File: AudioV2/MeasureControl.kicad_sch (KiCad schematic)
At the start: 107 parts, among them J1601 AUDIO, J1602 V_IN, J1603 15_V_IN, SW1601 DEST sense (3PDT 3rd pole, sa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, U1601 OPA1656, U1602 OPA1656, U1603 LT1763-3.3, U1605 TPS3307-33, U1606 LT1763-5, U1607 BP5293-50, U1608 OPA1656, U1609 XC8107AC20MR-G, U1610 MCP23017 (UI 0x22), U1611 OPA1656, Y1601 ASFL1-12.288MHZ-EC-T

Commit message: AudioV2: HP バッファを移設し、PT2314E の DGND を A_GND へ寄せて I²C にレベルシフタを入れた
未実装のまま「確定」に留まっていた2件を回路図に入れ、注釈・BOM の腐りを直した。

- HP バッファ移設（2026-09-06 確定）: legacy/OutputStage に U501（DIP-8 ソケット、
  標準実装 OPA1652）+ R501/R502 10Ω + C501/C502 470µF NP + R503/R504 100k +
  C503-C506。RV501 ワイパー側のラベルを PHONE_BUF_L/R に改名し、PHONE_L/R は
  バッファ出力になった。J_HP501 / J_LINE501 を 01x03（L / A_GND / R）にして帰路を入れた
- DGND→A_GND ＋ I²C 境界（2026-09-07 確定）: U402.25 を A_GND へ。境界は BSS138 ×2 の
  双方向レベルシフタ（Q401/Q402、PT 側 R412/R413 10k → VCC_TONE）。P82B96 を使わない
  理由（Sx 側 VOL 0.8–1.0 V が PT2314E VIL 1.0 V / RP2350 VIL 0.8 V を食い切る）は
  DECISIONS の実装節に一次資料の数字で置いた
- MeasureControl の注釈: 上書きしてしまった Pico ピン配置ノートを復元（GP9=NC）、
  R1605 / 3.3k の旧記述を消し、U1611 Description を実値（約30k・−115.5 dB）に直した
- NT1603 を in_bom no に揃え、PARTS.md は 385（ネットリスト 389 − NetTie 4）
- DECISIONS: PPTC「戻さない」の理由を言い直し（1・2行目は判定材料にならない、
  3行目の条件は X7R 割れに限らない、U201 の OCP は 230 % max @ nom. VIN 24 V）、
  ヘッドルーム −0.4 dBFS は typ 基準で余裕の確定ではないと追記（7.5k 案を併記）、
  U1611 の 47Ω 省略に CL 100 pF の根拠を足した

検証: check_sexpr 0 / roundtrip 全 OK / 再生成は冪等（バイト一致）/ ERC 11 件（型・件数とも
変化なし）/ ネットリスト 389 個・重複 0・フットプリント未設定 0 / 母板で座標の偶然一致なし

Co-Authored-By: Claude Fable 5.1 <noreply@anthropic.com>
Claude-Session: https://claude.ai/code/session_01VCArLcCGbMGgxvWJ5HFJiY
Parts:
- NT1603: now left out of the parts list
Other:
- note added: "A3 Pico2 横置き: 南列 1-20 西→東 / 北列 21-40 東→西。VSYS=+5V_D via D1601 ショットキ, GND=D_GND | GP0=ADC_DATA GP1=ADC_BCK GP2=ADC_LRCK | GP3/GP4=NC(旧 LCD SPI) | GP5=LCD_CS GP6=LCD_DC GP7=LCD_RST GP8=LCD_EN | GP9=NC（旧 MCLK_SENSE、2026-09-07 削除） | GP10=TP_SDA GP11=TP_SCL GP12=TP_INT GP13=TP_RST | GP15=ADC_nMR (TPS3307 ~MR, OD, H は駆動しない) | GP16=ENC_INTA GP17=ENC_INTB (U1610 MCP23017 割り込み) | GP18=LCD_SCK GP19=LCD_MOS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"
- note added: "OPA2134 からの OPA1656 置き換え。6.19k/4.7k 網（前段入力抵抗は 2026-09-07 に 3.3k→6.19k）では FET 入力が有利。試作で安定性とフルスケール・レベルを確認すること。"
- note added: "POWER/DIGITAL（2026-09-07）: +15V → U1603(+3V3_A) と U1606(+5V_A, SHDN=+3V3_A)。旧 U1604(MBC2596) は削除。U1607=+5V_D（PD_12V_MEAS から）。D1601 ショットキ: +5V_D → Pico VSYS（USB 逆流止め）。Y1601 12.288MHz → R1604 33Ω → SCKI。U1609 XC8107 → LCD_VCC。U1605 TPS3307 監視。"
- note removed: "OPA2134 からの OPA1656 置き換え。3.3k/4.7k 網では FET 入力が有利。試作で安定性とフルスケール・レベルを確認すること。"
- note removed: "POWER/DIGITAL（2026-09-07）: +15V → U1603(+3V3_A) と U1606(+5V_A, SHDN=+3V3_A)。旧 U1604(MBC2596) は削除。U1607=+5V_D（PD_12V_MEAS から）。D1601 ショットキ: +5V_D → Pico VSYS（USB 逆流止め）。Y1601 12.288MHz → R1604 33Ω → SCKI。R1605 1k → MCLK_SENSE(GP9、監視のみ。⚠ ファームは未使用)。U1609 XC8107 → LCD_VCC。U1605 TPS3307 監視。"
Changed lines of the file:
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@@
 		)
 	)
-	(text "POWER/DIGITAL（2026-09-07）: +15V → U1603(+3V3_A) と U1606(+5V_A, SHDN=+3V3_A)。旧 U1604(MBC2596) は削除。U1607=+5V_D（PD_12V_MEAS から）。D1601 ショットキ: +5V_D → Pico VSYS（USB 逆流止め）。Y1601 12.288MHz → R1604 33Ω → SCKI。R1605 1k → MCLK_SENSE(GP9、監視のみ。⚠ ファームは未使用)。U1609 XC8107 → LCD_VCC。U1605 TPS3307 監視。"
+	(text "POWER/DIGITAL（2026-09-07）: +15V → U1603(+3V3_A) と U1606(+5V_A, SHDN=+3V3_A)。旧 U1604(MBC2596) は削除。U1607=+5V_D（PD_12V_MEAS から）。D1601 ショットキ: +5V_D → Pico VSYS（USB 逆流止め）。Y1601 12.288MHz → R1604 33Ω → SCKI。U1609 XC8107 → LCD_VCC。U1605 TPS3307 監視。"
 		(exclude_from_sim no)
 		(at 325.12 17.78 0)
@@
 		)
 	)
-	(text "GP9: 旧 MCLK_SENSE（R1605 1k 経由）は 2026-09-07 に削除。ファームは GP9 を読んでいなかった。SCKI の生死は BCK（=SCKI/4）で分かる。GP9 は no_connect。"
+	(text "A3 Pico2 横置き: 南列 1-20 西→東 / 北列 21-40 東→西。VSYS=+5V_D via D1601 ショットキ, GND=D_GND | GP0=ADC_DATA GP1=ADC_BCK GP2=ADC_LRCK | GP3/GP4=NC(旧 LCD SPI) | GP5=LCD_CS GP6=LCD_DC GP7=LCD_RST GP8=LCD_EN | GP9=NC（旧 MCLK_SENSE、2026-09-07 削除） | GP10=TP_SDA GP11=TP_SCL GP12=TP_INT GP13=TP_RST | GP15=ADC_nMR (TPS3307 ~MR, OD, H は駆動しない) | GP16=ENC_INTA GP17=ENC_INTB (U1610 MCP23017 割り込み) | GP18=LCD_SCK GP19=LCD_MOSI (SPI0)"
 		(exclude_from_sim no)
 		(at 171.45 213.36 0)
@@
 		)
 	)
-	(text "OPA2134 からの OPA1656 置き換え。3.3k/4.7k 網では FET 入力が有利。試作で安定性とフルスケール・レベルを確認すること。"
+	(text "OPA2134 からの OPA1656 置き換え。6.19k/4.7k 網（前段入力抵抗は 2026-09-07 に 3.3k→6.19k）では FET 入力が有利。試作で安定性とフルスケール・レベルを確認すること。"
 		(exclude_from_sim no)
 		(at 20.32 81.28 0)
@@
 		(body_style 1)
 		(exclude_from_sim no)
-		(in_bom yes)
+		(in_bom no)
 		(on_board yes)
 		(in_pos_files yes)
@@
 			)
 		)
-		(property "Description" "計測タップの「+」側バッファ（v1 の AdcBuffer を復元）。ユニティフォロワ、入力 100k→A_GND。音声バスから見た負荷を 1.87k→100k に戻し、両ブランチが 10µF を見る源インピーダンスを揃える（Vg 除去 20Hz 10.5→43dB、TMUX7612 の H3 −94.9→−119.7dB、低域 39→17Hz）。v1 の出力 47Ω は対称性のため付けない。2026-09-07"
+		(property "Description" "計測タップの「+」側バッファ（v1 の AdcBuffer を復元）。ユニティフォロワ、入力 100k→A_GND。音声バスから見た負荷を 1.87k→約30k（RV501 50k ∥ R603 220k ∥ R1659 100k）に戻し、両ブランチが 10µF を見る源インピーダンスを揃える（Vg 除去 20Hz 10.5→43dB、TMUX7612 の H3 −94.9→−115.5dB（spice/switch_thd.py --rload 30.4e3 実測）、低域 39→17Hz）。v1 の出力 47Ω は対称性のため付けない（負荷は R1612/R1614 系の抵抗で容量性ではなく、OPA1656 は CL 100 pF まで規定内。DS Electrical Characteristics）。2026-09-07"
 			(at 20.32 115.57 0)
 			(hide yes)
@@
 			)
 		)
-		(property "Description" "計測タップの「+」側バッファ（v1 の AdcBuffer を復元）。ユニティフォロワ、入力 100k→A_GND。音声バスから見た負荷を 1.87k→100k に戻し、両ブランチが 10µF を見る源インピーダンスを揃える（Vg 除去 20Hz 10.5→43dB、TMUX7612 の H3 −94.9→−119.7dB、低域 39→17Hz）。v1 の出力 47Ω は対称性のため付けない。2026-09-07"
+		(property "Description" "計測タップの「+」側バッファ（v1 の AdcBuffer を復元）。ユニティフォロワ、入力 100k→A_GND。音声バスから見た負荷を 1.87k→約30k（RV501 50k ∥ R603 220k ∥ R1659 100k）に戻し、両ブランチが 10µF を見る源インピーダンスを揃える（Vg 除去 20Hz 10.5→43dB、TMUX7612 の H3 −94.9→−115.5dB（spice/switch_thd.py --rload 30.4e3 実測）、低域 39→17Hz）。v1 の出力 47Ω は対称性のため付けない（負荷は R1612/R1614 系の抵抗で容量性ではなく、OPA1656 は CL 100 pF まで規定内。DS Electrical Characteristics）。2026-09-07"
 			(at 20.32 41.91 0)
 			(hide yes)
@@
 			)
 		)
-		(property "Description" "計測タップの「+」側バッファ（v1 の AdcBuffer を復元）。ユニティフォロワ、入力 100k→A_GND。音声バスから見た負荷を 1.87k→100k に戻し、両ブランチが 10µF を見る源インピーダンスを揃える（Vg 除去 20Hz 10.5→43dB、TMUX7612 の H3 −94.9→−119.7dB、低域 39→17Hz）。v1 の出力 47Ω は対称性のため付けない。2026-09-07"
+		(property "Description" "計測タップの「+」側バッファ（v1 の AdcBuffer を復元）。ユニティフォロワ、入力 100k→A_GND。音声バスから見た負荷を 1.87k→約30k（RV501 50k ∥ R603 220k ∥ R1659 100k）に戻し、両ブランチが 10µF を見る源インピーダンスを揃える（Vg 除去 20Hz 10.5→43dB、TMUX7612 の H3 −94.9→−115.5dB（spice/switch_thd.py --rload 30.4e3 実測）、低域 39→17Hz）。v1 の出力 47Ω は対称性のため付けない（負荷は R1612/R1614 系の抵抗で容量性ではなく、OPA1656 は CL 100 pF まで規定内。DS Electrical Characteristics）。2026-09-07"
 			(at 20.32 135.89 0)
 			(hide yes)

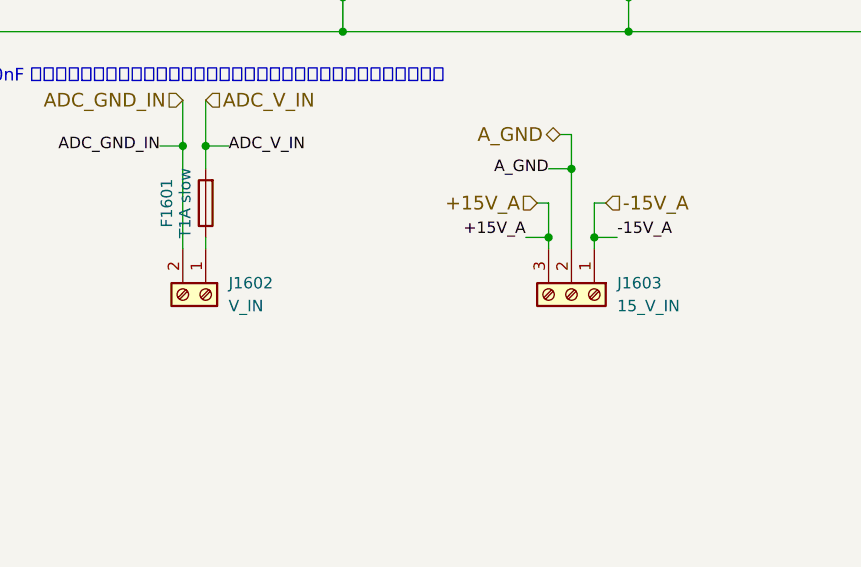
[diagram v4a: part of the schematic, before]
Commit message: AudioV2: J1602 / J1603 のピン並びを母板の J202 / J201 に揃えた
計測側の電源端子が母板側と逆順だった（J1603: -15/GND/+15 vs J201: +15/A_GND/-15、
J1602: +12V/GND vs J202: GND/+12V）。配線・ラベル・F1601 は動かさず、シンボルを
左右ミラーしてピンの x を入れ替えた（J1602 はアンカーも 1 ピッチ移動）。
J201 の Value「+15/-15/A_GND out」を実ピン順「+15/A_GND/-15 out」に直した（素材 → 再生成）。
端子を残すか外すかは B5 のハーネス判断のまま。J1601（AUDIO、R/L 2P）は J_RAIL501（L/A_GND/R 3P）
と形が違う点を NOW に書いた。

検証: kicad-cli ネットリストで J1603 1=+15V 2=A_GND 3=-15V、J1602 1=PD_GND 2=F1601 側を確認。
ERC 11 件（変化なし）・部品 389・重複 0・check_sexpr 0・roundtrip OK・再生成バイト一致。

Co-Authored-By: Claude Fable 5.1 <noreply@anthropic.com>
Claude-Session: https://claude.ai/code/session_01VCArLcCGbMGgxvWJ5HFJiY
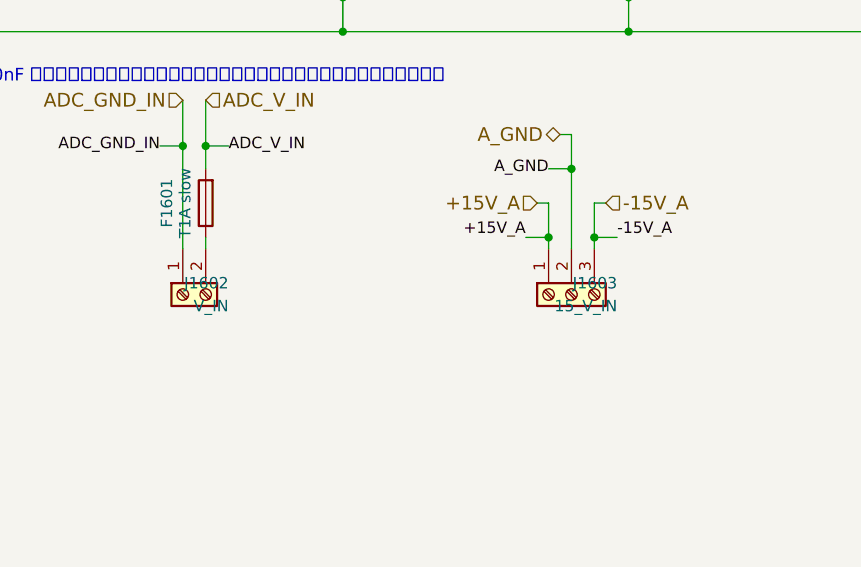
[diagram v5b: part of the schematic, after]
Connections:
- net +15V_A: now also J1603.1 (Pin_1); no longer J1603.3 (Pin_3)
- net -15V_A: now also J1603.3 (Pin_3); no longer J1603.1 (Pin_1)
- net ADC_GND_IN: now also J1602.1 (Pin_1); no longer J1602.2 (Pin_2)
- net at F1601.1: now also J1602.2 (Pin_2); no longer J1602.1 (Pin_1)
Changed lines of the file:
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@@
 	(symbol
 		(lib_id "Connector:Screw_Terminal_01x02")
-		(at 66.04 233.68 270)
+		(at 63.5 233.68 270)
+		(mirror y)
 		(unit 1)
 		(body_style 1)
@@
 			)
 		)
-		(property "Description" "Generic screw terminal, single row, 01x02, script generated (kicad-library-utils/schlib/autogen/connector/)"
+		(property "Description" "計測側の 12V 入口（F1601 経由で U1607 へ）。1=PD_GND / 2=+12V —— 母板 J202（1=GND 2=+12V）と同じ並び。2026-09-09 に揃えた。残すか外すかは B5 のハーネス判断"
 			(at 66.04 233.68 0)
 			(hide yes)
@@
 		(lib_id "Connector:Screw_Terminal_01x03")
 		(at 106.68 233.68 270)
+		(mirror y)
 		(unit 1)
 		(body_style 1)
@@
 			)
 		)
-		(property "Description" "Generic screw terminal, single row, 01x03, script generated (kicad-library-utils/schlib/autogen/connector/)"
+		(property "Description" "計測側の ±15V 入口。1=+15V_A / 2=A_GND / 3=-15V_A —— 母板 J201（+15/A_GND/-15）と同じ並び。2026-09-09 にミラーで揃えた（それまで逆だった）。残すか外すかは B5 のハーネス判断"
 			(at 106.68 233.68 0)
 			(hide yes)

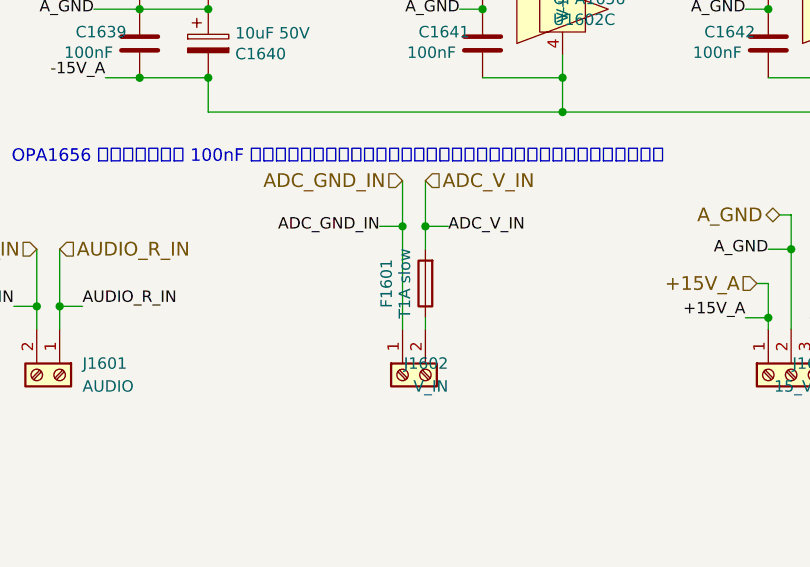
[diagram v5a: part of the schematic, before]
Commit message: AudioV2: ヒューズ / PPTC を入手性で型番決めし、5 個の FP を軸リードから実物に差し替えた
査読の指摘「F201 は Value 5×20 なのに FP が軸リード。他の 4 個も同じ」を潰した。

- 5×20 ガラス管（F201 T1.6A、F1601 T1A）: ホルダ Schurter OGN 0031.8201（DigiKey 在庫 6 万・¥240）。
  FP は KiCad 標準 Fuseholder_Cylinder-5x20mm_Schurter_0031_8201_Horizontal_Open
- PPTC（F202 / F203 / F1602）: Littelfuse RXEF040 / RXEF010 / RXEF050（在庫 2〜8 万）。
  Bourns MF-R040 / 010 / 050 も同寸で挿さる。F202 は 0.35 A の品が両社に無いので 0.40 A に寄せた
  （コイル枝のピークは約 0.16 A）。FP は Library:PPTC_Radial_D7.9mm_T3.1mm_P5.08mm を新設
  （DigiKey パラメータ: φ7.4〜7.9 × 3.0〜3.1、リード間隔 5.05 / 5.10。メーカー DS は 403 で未取得。
  穴 1.1 でピッチの差を吸収）
- 各 F の Description に型番と理由、PARTS.md の手書き行と NOW.md を更新

検証: 再生成バイト一致・check_sexpr 0（新 FP も）・kicad-cli fp export で FP 読込 OK・roundtrip OK・
ERC 11 件（変化なし）・部品 389・重複 0・フットプリント未設定 0

Co-Authored-By: Claude Fable 5.1 <noreply@anthropic.com>
Claude-Session: https://claude.ai/code/session_01VCArLcCGbMGgxvWJ5HFJiY
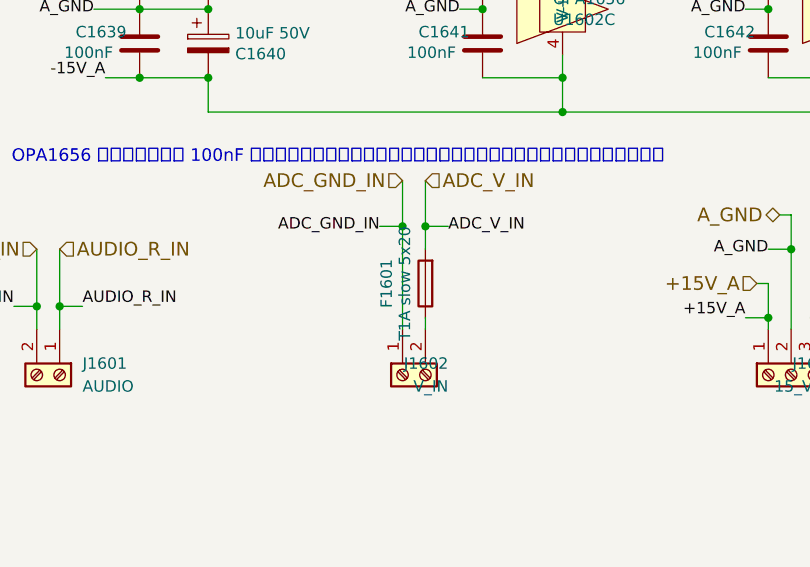
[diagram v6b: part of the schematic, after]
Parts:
- F1601: value T1A slow -> T1A slow 5x20; footprint Resistor_THT:R_Axial_DIN0411_L9.9mm_D3.6mm_P12.70mm_Horizontal -> Fuse:Fuseholder_Cylinder-5x20mm_Schurter_0031_8201_Horizontal_Open
- F1602: footprint Resistor_THT:R_Axial_DIN0411_L9.9mm_D3.6mm_P12.70mm_Horizontal -> Library:PPTC_Radial_D7.9mm_T3.1mm_P5.08mm
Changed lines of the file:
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@@
 			)
 		)
-		(property "Value" "T1A slow"
+		(property "Value" "T1A slow 5x20"
 			(at 63.754 223.52 90)
 			(show_name no)
@@
 			)
 		)
-		(property "Footprint" "Resistor_THT:R_Axial_DIN0411_L9.9mm_D3.6mm_P12.70mm_Horizontal"
+		(property "Footprint" "Fuse:Fuseholder_Cylinder-5x20mm_Schurter_0031_8201_Horizontal_Open"
 			(at 67.818 223.52 90)
 			(hide yes)
@@
 			)
 		)
-		(property "Description" "Fuse"
+		(property "Description" "計測側 12V 入口（J1602）のヒューズ。J1602 を外すなら一緒に消える。ホルダは Schurter OGN 0031.8201（基板用 5×20 オープン型、DigiKey 在庫 6 万・¥240、KiCad 標準 FP）。中身は 5×20 ガラス管スローブロー T1A（例: Bel 0652C1000/1600-11、Littelfuse 0218 系、秋月の 5.2×20 スロー品も挿さる）。2026-09-09 に軸リード FP からホルダ FP へ直した"
 			(at 66.04 223.52 0)
 			(hide yes)
@@
 			)
 		)
-		(property "Footprint" "Resistor_THT:R_Axial_DIN0411_L9.9mm_D3.6mm_P12.70mm_Horizontal"
+		(property "Footprint" "Library:PPTC_Radial_D7.9mm_T3.1mm_P5.08mm"
 			(at 67.818 223.52 90)
 			(hide yes)
@@
 			)
 		)
-		(property "Description" "Fuse"
+		(property "Description" "計測側 +5V_D（U1607）入口の PPTC。ラジアル PPTC。Littelfuse RXEF050（Ih 0.50 A / It 1.0 A / 72 V）。Bourns MF-R050 も同寸で可。FP は DigiKey の寸法（φ7.4〜7.9×3.1、ピッチ 5.05〜5.10）から起こした Library の自作。2026-09-09 に軸リード FP から直した"
 			(at 66.04 223.52 0)
 			(hide yes)
